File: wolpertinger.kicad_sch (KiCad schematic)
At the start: 117 parts, among them J1 RIGHT IN, J2 LEFT IN, J3 EXT LFO, J4 LEFT OUT, J5 RIGHT OUT, J6 Jack-DC, K1 FRT5, K2 FRT5, Q1 BC549, Q2 BC547, Q3 BC547, SW1 ON/OFF, SW2 DPDT MONO/STEREO, SW3 DPDT HARMONIC/TREMOLO, U1 4093, U10 L78L05_TO92, U2 TL074, U3 TL074, U4 NE5532, U5 VTL5C, U6 VTL5C, U7 VTL5C, U8 VTL5C, U9 NE5532

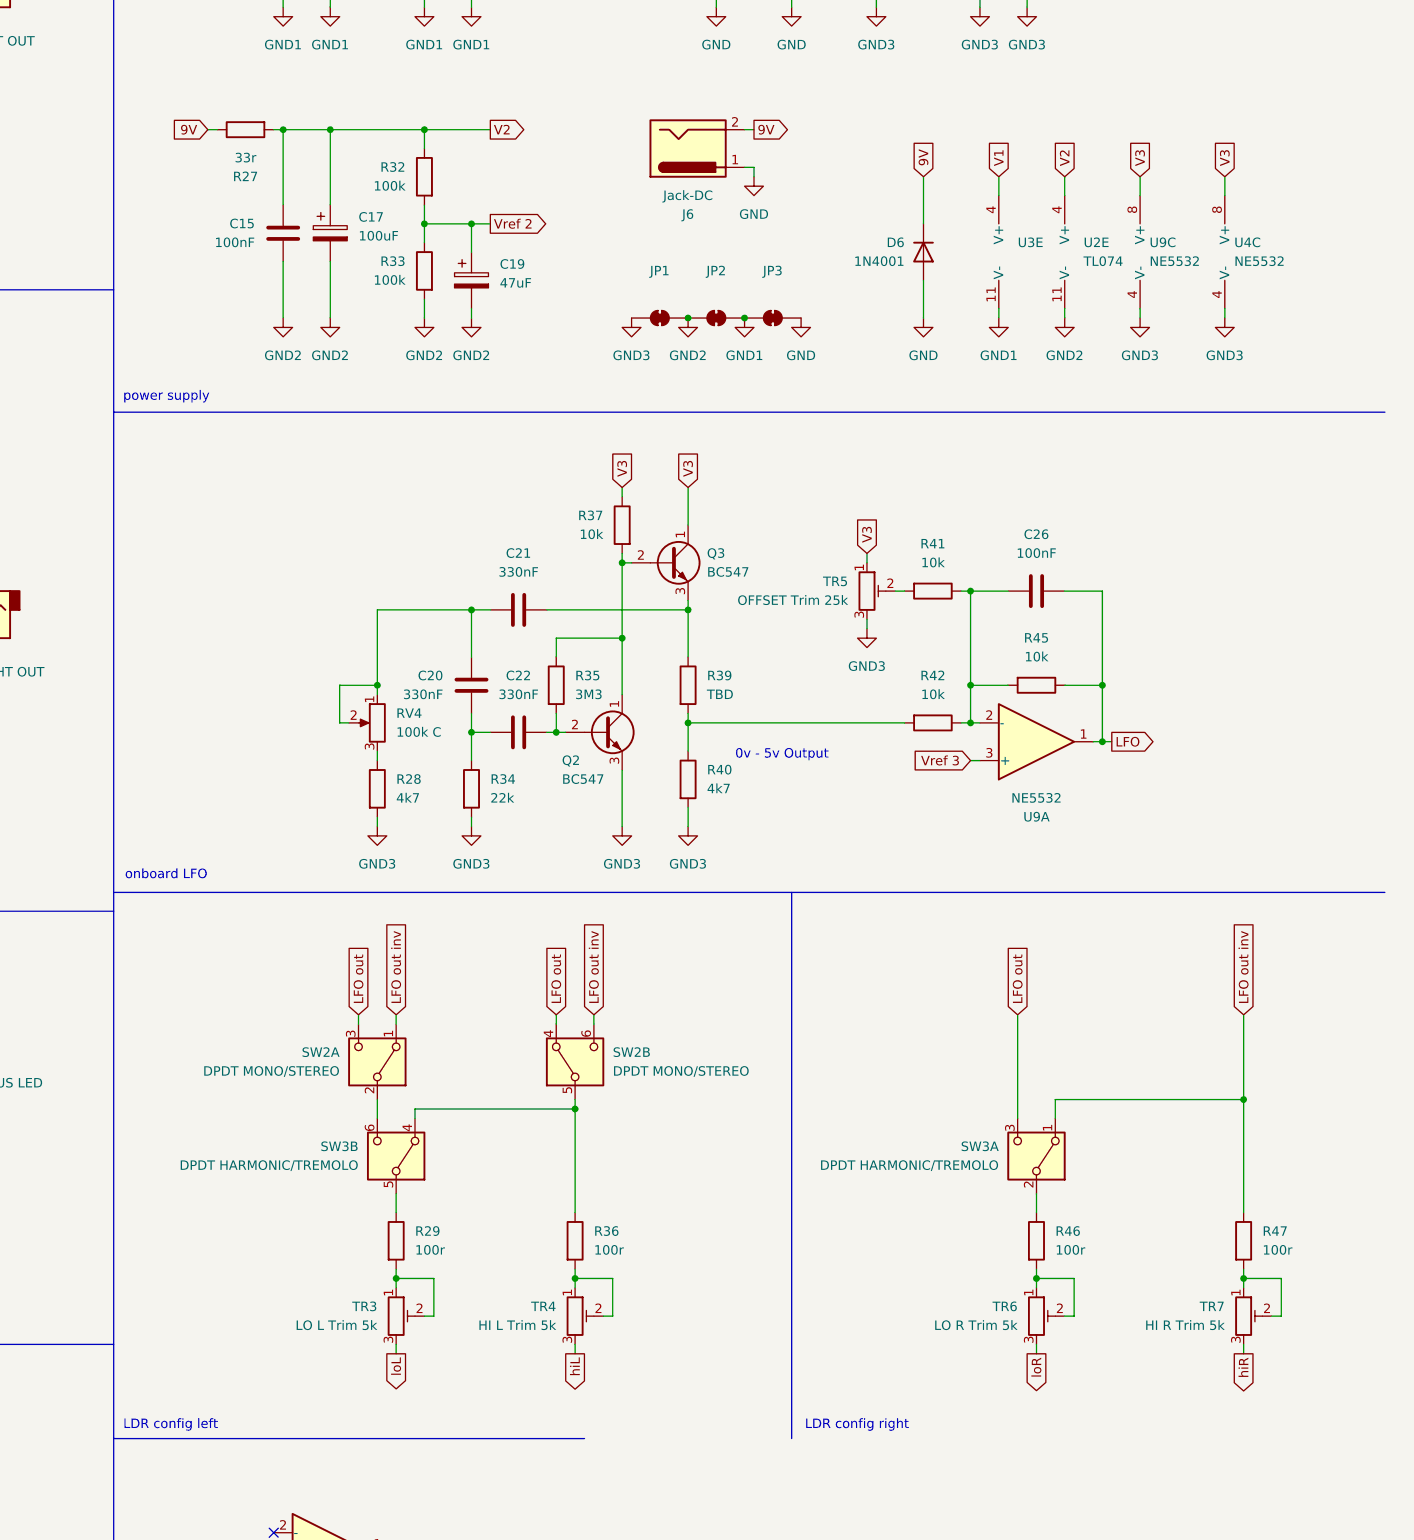
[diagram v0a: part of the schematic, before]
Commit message: Left channel layout
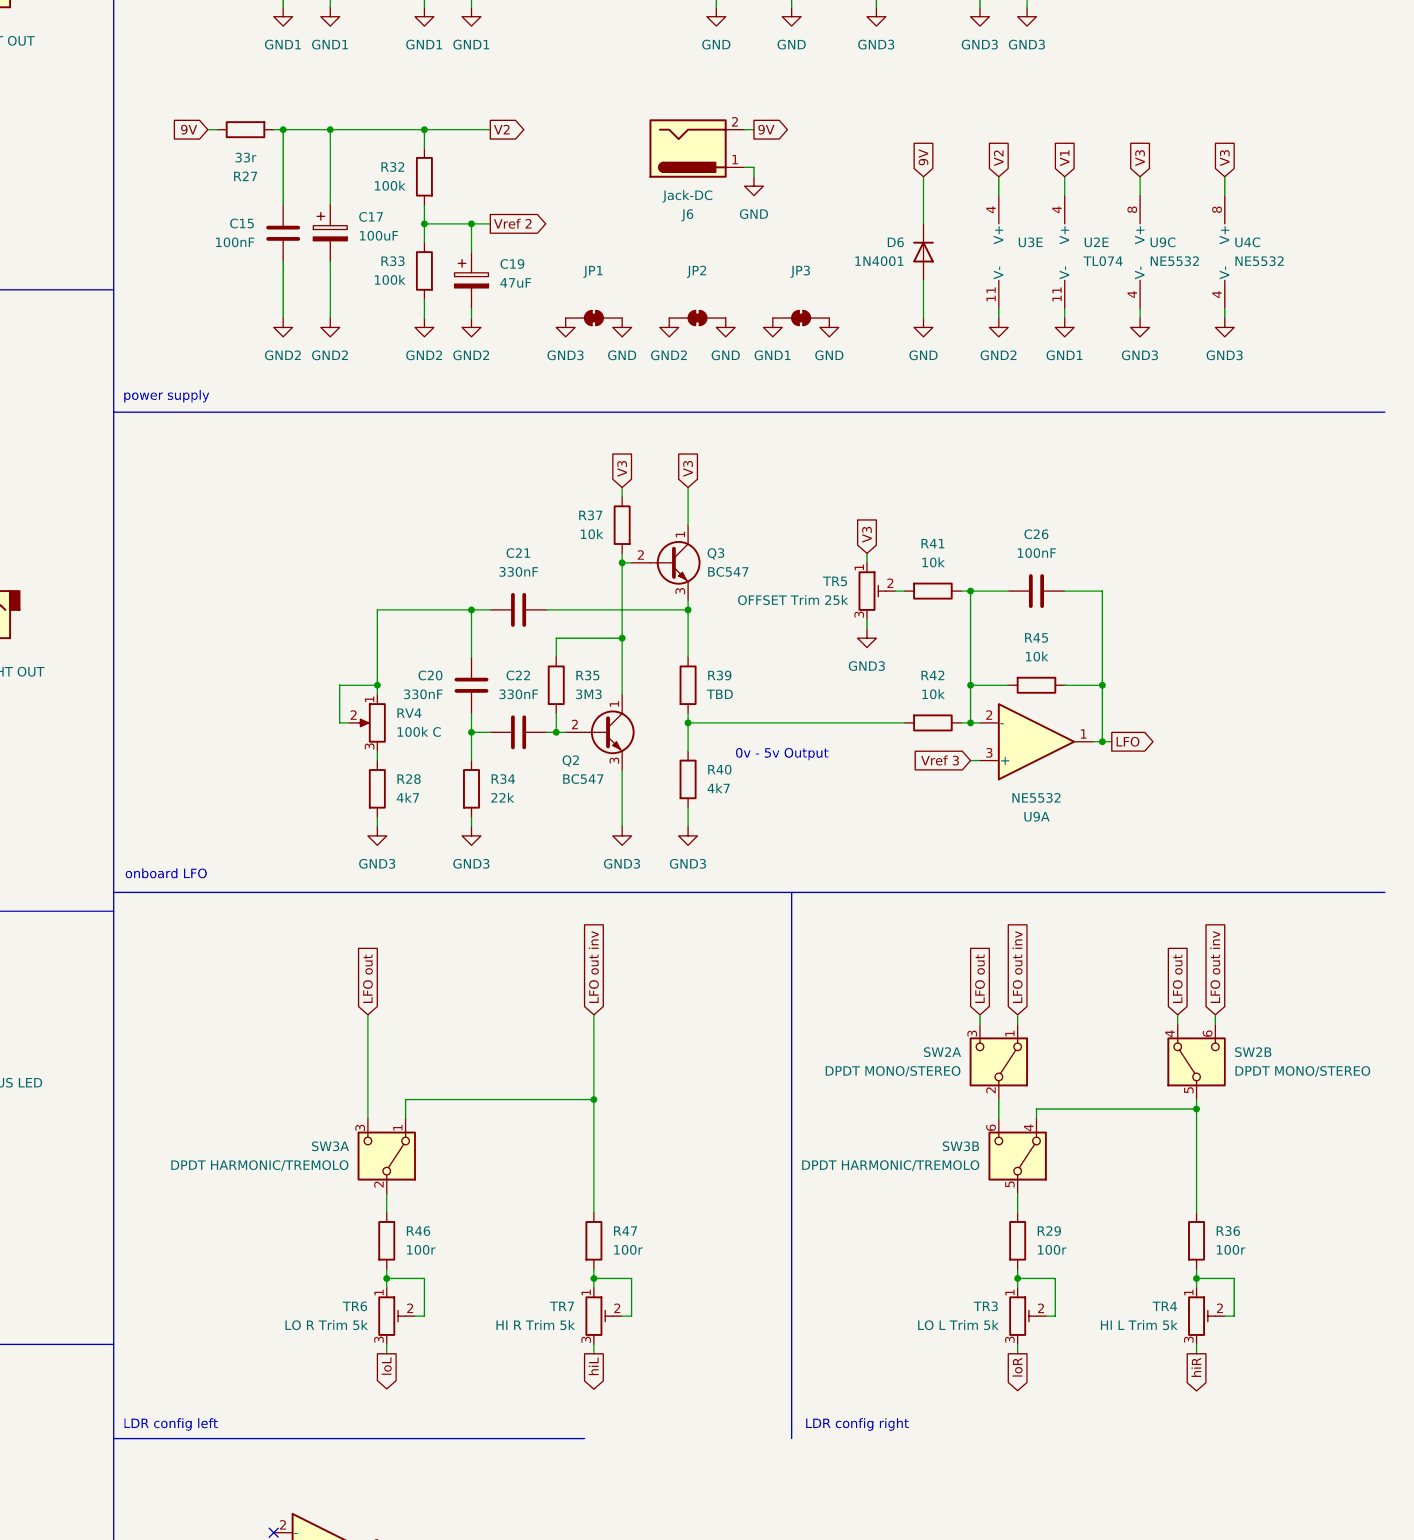
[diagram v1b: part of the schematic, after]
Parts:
- J6: footprint (none) -> jacks:BATTERY
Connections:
- net GND: now also JP1.2 (B), JP2.2 (B)
- net GND1: now also U2.11 (V-); no longer JP2.2 (B), U3.11 (V-)
- net GND2: now also U3.11 (V-); no longer JP1.2 (B), U2.11 (V-)
- net V1: now also U2.4 (V+); no longer U3.4 (V+)
- net V2: now also U3.4 (V+); no longer U2.4 (V+)
- net hiL: now also TR7.3; no longer TR4.3
- net hiR: now also TR4.3; no longer TR7.3
- net loL: now also TR6.3; no longer TR3.3
- net loR: now also TR3.3; no longer TR6.3
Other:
- moved on the sheet: JP1, JP2, JP3, R29, R36, R46, R47, SW2A, SW2B, SW3A, SW3B, TR3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

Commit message: populate pcb
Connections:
- net BYPASS R: now also K2.4, K2.9; no longer K2.2, K2.7
- net GND2: now also K2.2; no longer K2.9
- net Vref2: now also U3.3 (+); no longer U3.12 (+)
- net hiL: now also TR4.3; no longer TR7.3
- net hiR: now also TR7.3; no longer TR4.3
- net loL: now also TR3.3; no longer TR6.3
- net loR: now also TR6.3; no longer TR3.3
- net at J5.T: now also K2.8; no longer K2.3
- net at C13.2, R24.1: now also K2.7; no longer K2.4
- net at TR2.3, U7.4, U8.4: now also U3.2 (-); no longer U3.13 (-)
- net at C13.1, TR2.1, TR2.2: now also U3.1; no longer U3.14
- net at C3.1, R2.1: now also K2.3; no longer K2.8
- net at C3.2, R4.2: now also U3.12 (+); no longer U3.3 (+)
- new net: C6.1, U3.13 (-), U3.14
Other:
- moved on the sheet: R29, R36, R46, R47, SW2A, SW2B, SW3A, SW3B, TR3, TR4, TR6, TR7

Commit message: layout work
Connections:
- net Vref 1 is gone; now on net Vref1: C18.1, R30.2, R31.1
- net Vref 2 is gone; now on net Vref2: C19.1, R32.2, R33.1
- net Vref 3 renamed Vref3
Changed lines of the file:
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@@
 		)
 	)
-	(global_label "Vref 1"
+	(global_label "Vref1"
 		(shape output)
 		(at 287.02 46.99 0)
@@
 		)
 		(property "Intersheetrefs" "${INTERSHEET_REFS}"
-			(at 295.8714 46.99 0)
+			(at 294.9038 46.99 0)
 			(effects
 				(font
@@
 		)
 	)
-	(global_label "Vref 2"
+	(global_label "Vref2"
 		(shape output)
 		(at 287.02 88.9 0)
@@
 		)
 		(property "Intersheetrefs" "${INTERSHEET_REFS}"
-			(at 295.8714 88.9 0)
+			(at 294.9038 88.9 0)
 			(effects
 				(font
@@
 		)
 	)
-	(global_label "Vref 3"
+	(global_label "Vref3"
 		(shape output)
 		(at 361.95 46.99 0)
@@
 		)
 		(property "Intersheetrefs" "${INTERSHEET_REFS}"
-			(at 370.8014 46.99 0)
+			(at 369.8338 46.99 0)
 			(effects
 				(font
@@
 		)
 	)
-	(global_label "Vref 3"
+	(global_label "Vref3"
 		(shape input)
 		(at 351.79 161.29 180)
@@
 		)
 		(property "Intersheetrefs" "${INTERSHEET_REFS}"
-			(at 342.9386 161.29 0)
+			(at 343.9062 161.29 0)
 			(effects
 				(font
@@
 		)
 	)
-	(global_label "Vref 3"
+	(global_label "Vref3"
 		(shape input)
 		(at 99.06 273.05 270)
@@
 		)
 		(property "Intersheetrefs" "${INTERSHEET_REFS}"
-			(at 99.06 281.9014 90)
+			(at 99.06 280.9338 90)
 			(effects
 				(font
@@
 		)
 	)
-	(global_label "Vref 3"
+	(global_label "Vref3"
 		(shape input)
 		(at 153.67 265.43 180)
@@
 		)
 		(property "Intersheetrefs" "${INTERSHEET_REFS}"
-			(at 144.8186 265.43 0)
-			(effects
-				(font
+			(at 145.7862 265.43 0)
+			(effects
+				(font

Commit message: add wide transistor footprint
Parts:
- Q1, Q2, Q3, U10: footprint Package_TO_SOT_THT:TO-92_Inline -> Package_TO_SOT_THT:TO-92_Inline_Wide
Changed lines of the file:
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@@
 			)
 		)
-		(property "Footprint" "Package_TO_SOT_THT:TO-92_Inline"
+		(property "Footprint" "Package_TO_SOT_THT:TO-92_Inline_Wide"
 			(at 327.66 28.575 0)
 			(effects
@@
 			)
 		)
-		(property "Footprint" "Package_TO_SOT_THT:TO-92_Inline"
+		(property "Footprint" "Package_TO_SOT_THT:TO-92_Inline_Wide"
 			(at 307.34 159.385 0)
 			(effects
@@
 			)
 		)
-		(property "Footprint" "Package_TO_SOT_THT:TO-92_Inline"
+		(property "Footprint" "Package_TO_SOT_THT:TO-92_Inline_Wide"
 			(at 316.23 136.525 0)
 			(effects
@@
 			)
 		)
-		(property "Footprint" "Package_TO_SOT_THT:TO-92_Inline"
+		(property "Footprint" "Package_TO_SOT_THT:TO-92_Inline_Wide"
 			(at 200.66 226.695 0)
 			(effects

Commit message: GND improvements
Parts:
- added JP4: ~, Jumper:SolderJumper-2_P1.3mm_Bridged_RoundedPad1.0x1.5mm, symbol Jumper:SolderJumper_2_Bridged
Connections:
- net GND: now also JP4.2 (B); no longer C1.2, C23.2, C7.2, D5.1 (K), Q1.3 (E), U1.12, U1.13, U1.7 (Vss), U1.7 (Vss), U1.7 (Vss), U1.7 (Vss), U1.8, U1.9
- net GND3: now also C23.2, D5.1 (K)
- new net GND4: C1.2, C7.2, JP4.1 (A), Q1.3 (E), U1.12, U1.13, U1.7 (Vss), U1.7 (Vss), U1.7 (Vss), U1.7 (Vss), U1.8, U1.9
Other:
- moved on the sheet: C23, C24, C25, D5, D6, J6, JP1, JP2, JP3, R38, R43, R44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
